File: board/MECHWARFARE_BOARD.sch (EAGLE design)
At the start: 8 parts, among them J1 5267-3, Q2 FDD4141TO252

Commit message: giving access to necessary libs
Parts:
- removed MS1: FEATHERWINGEXTENDED_BOTH_ENDS, ME507:FEATHERWINGEXTENDED_BOTH_ENDS
- removed TURRET_PWR1: XT60, XT60:XT60
- added MS2: FEATHERWINGEXTENDED_BOTH_ENDS, ME507:FEATHERWINGEXTENDED_BOTH_ENDS
- added U$1: XT60, XT60:XT60
- renumbered J1 to J2, TURRET_PWR to U$2
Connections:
- net GND: now also MS2.GND, U$1.GND; no longer MS1.GND, TURRET_PWR1.GND
- net MOTOR_CMD: now also MS2.GPIOTX; no longer MS1.GPIOTX
- net MOTOR_POWER: now also U$1.VCC; no longer TURRET_PWR1.VCC
- net N$21: now also MS2.GPIO5; no longer MS1.GPIO5
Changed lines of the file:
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@@
 </classes>
 <parts>
-<part name="FRAME1" library="ME507" deviceset="TITLEBLOCK_LET_L" device="">
-<attribute name="BOARD_NAME" value="ZEN GARDEN"/>
-</part>
 <part name="R1" library="rcl" library_urn="urn:adsk.eagle:library:334" deviceset="R-US_" device="R0805" package3d_urn="urn:adsk.eagle:package:23553/2" value="100"/>
 <part name="X_1" library="ngspice-simulation" library_urn="urn:adsk.eagle:library:527439" deviceset="GND" device=""/>
 <part name="D1" library="diode" library_urn="urn:adsk.eagle:library:210" deviceset="DIODE-" device="DO-214AC" package3d_urn="urn:adsk.eagle:package:43416/2"/>
-<part name="MS1" library="ME507" deviceset="FEATHERWING" device="EXTENDED_BOTH_ENDS"/>
-<part name="TURRET_PWR" library="XT60" deviceset="XT60" device=""/>
 <part name="X_2" library="ngspice-simulation" library_urn="urn:adsk.eagle:library:527439" deviceset="GND" device=""/>
 <part name="Q2" library="transistor-fet" library_urn="urn:adsk.eagle:library:396" deviceset="FDD4141" device="TO252" package3d_urn="urn:adsk.eagle:package:28537/2"/>
-<part name="TURRET_PWR1" library="XT60" deviceset="XT60" device=""/>
 <part name="X_3" library="ngspice-simulation" library_urn="urn:adsk.eagle:library:527439" deviceset="GND" device=""/>
 <part name="X3" library="ME507" deviceset="SCREWTERM_2P" device="_254"/>
 <part name="X_5" library="ngspice-simulation" library_urn="urn:adsk.eagle:library:527439" deviceset="GND" device=""/>
 <part name="X_4" library="ngspice-simulation" library_urn="urn:adsk.eagle:library:527439" deviceset="GND" device=""/>
-<part name="J1" library="con-molex-spox" deviceset="5267-3" device=""/>
+<part name="U$1" library="XT60" deviceset="XT60" device=""/>
+<part name="U$2" library="XT60" deviceset="XT60" device=""/>
+<part name="J2" library="con-molex-spox" deviceset="5267-3" device=""/>
+<part name="MS2" library="ME507" deviceset="FEATHERWING" device="EXTENDED_BOTH_ENDS"/>
+<part name="FRAME1" library="ME507" deviceset="TITLEBLOCK_LET_L" device="">
+<attribute name="AUTHOR" value="Aaron Tran"/>
+<attribute name="BOARD_NAME" value="MOT_AND_TURRET"/>
+<attribute name="PROJECT_NAME" value="MECH WARFARE"/>
+</part>
 </parts>
 <sheets>
@@
 </plain>
 <instances>
-<instance part="FRAME1" gate="G$3" x="0" y="0" smashed="yes"/>
-<instance part="FRAME1" gate="G$1" x="-5.08" y="0" smashed="yes"/>
-<instance part="FRAME1" gate="G$2" x="142.24" y="0" smashed="yes">
-<attribute name="LAST_DATE_TIME" x="154.94" y="11.43" size="2.54" layer="94"/>
-<attribute name="SHEET" x="184.15" y="6.35" size="2.54" layer="94"/>
-<attribute name="DRAWING_NAME" x="235.585" y="3.81" size="2.54" layer="94" align="bottom-right"/>
-<attribute name="REVISION" x="152.4" y="6.35" size="2.54" layer="94"/>
-<attribute name="PROJECT_NAME" x="160.02" y="30.48" size="2.54" layer="94"/>
-<attribute name="DOC_NUM" x="179.324" y="1.27" size="2.54" layer="94"/>
-<attribute name="AUTHOR" x="165.1" y="16.51" size="2.54" layer="94"/>
-<attribute name="BOARD_NAME" x="154.94" y="22.86" size="2.54" layer="94"/>
-</instance>
 <instance part="R1" gate="G$1" x="149.86" y="88.9" smashed="yes">
 <attribute name="NAME" x="146.05" y="90.3986" size="1.778" layer="95"/>
@@
 <attribute name="VALUE" x="190.2714" y="104.14" size="1.778" layer="96" rot="R90"/>
 </instance>
-<instance part="MS1" gate="G$1" x="96.52" y="127" smashed="yes" rot="R270"/>
-<instance part="TURRET_PWR" gate="G$1" x="175.26" y="116.84" smashed="yes" rot="R180"/>
 <instance part="X_2" gate="G$1" x="180.34" y="111.76" smashed="yes"/>
 <instance part="Q2" gate="G$1" x="185.42" y="86.36" smashed="yes">
@@
 <attribute name="NAME" x="173.99" y="85.09" size="1.778" layer="95"/>
 </instance>
-<instance part="TURRET_PWR1" gate="G$1" x="58.42" y="124.46" smashed="yes"/>
-<instance part="X_3" gate="G$1" x="38.1" y="124.46" smashed="yes"/>
+<instance part="X_3" gate="G$1" x="35.56" y="124.46" smashed="yes"/>
 <instance part="X3" gate="-1" x="231.14" y="104.14" smashed="yes">
 <attribute name="NAME" x="234.696" y="103.505" size="1.778" layer="95"/>
@@
 <instance part="X_5" gate="G$1" x="81.28" y="111.76" smashed="yes"/>
 <instance part="X_4" gate="G$1" x="33.02" y="101.6" smashed="yes"/>
-<instance part="J1" gate="G$1" x="38.1" y="88.9" smashed="yes" rot="R180">
+<instance part="U$1" gate="G$1" x="58.42" y="127" smashed="yes"/>
+<instance part="U$2" gate="G$1" x="175.26" y="116.84" smashed="yes" rot="R180"/>
+<instance part="J2" gate="G$1" x="38.1" y="88.9" smashed="yes" rot="R180">
 <attribute name="VALUE" x="38.1" y="94.38" size="1.27" layer="94" rot="R180"/>
 <attribute name="NAME" x="38.1" y="83.74" size="1.27" layer="94" rot="R180"/>
+</instance>
+<instance part="MS2" gate="G$1" x="99.06" y="127" smashed="yes" rot="R270"/>
+<instance part="FRAME1" gate="G$3" x="5.08" y="0" smashed="yes"/>
+<instance part="FRAME1" gate="G$1" x="0" y="0" smashed="yes"/>
+<instance part="FRAME1" gate="G$2" x="147.32" y="0" smashed="yes">
+<attribute name="LAST_DATE_TIME" x="160.02" y="11.43" size="2.54" layer="94"/>
+<attribute name="SHEET" x="189.23" y="6.35" size="2.54" layer="94"/>
+<attribute name="DRAWING_NAME" x="240.665" y="3.81" size="2.54" layer="94" align="bottom-right"/>
+<attribute name="REVISION" x="157.48" y="6.35" size="2.54" layer="94"/>
+<attribute name="PROJECT_NAME" x="165.1" y="30.48" size="2.54" layer="94"/>
+<attribute name="DOC_NUM" x="184.404" y="1.27" size="2.54" layer="94"/>
+<attribute name="AUTHOR" x="170.18" y="16.51" size="2.54" layer="94"/>
+<attribute name="BOARD_NAME" x="160.02" y="22.86" size="2.54" layer="94"/>
 </instance>
 </instances>
@@
 <label x="210.82" y="104.14" size="1.778" layer="95"/>
 <pinref part="D1" gate="G$1" pin="C"/>
-<pinref part="TURRET_PWR" gate="G$1" pin="VCC"/>
 <wire x1="203.2" y1="104.14" x2="228.6" y2="104.14" width="0.1524" layer="91"/>
 <wire x1="180.34" y1="119.38" x2="203.2" y2="119.38" width="0.1524" layer="91"/>
@@
 <junction x="203.2" y="104.14"/>
 <pinref part="X3" gate="-1" pin="1"/>
+<pinref part="U$2" gate="G$1" pin="VCC"/>
 </segment>
 </net>
@@
 </segment>
 <segment>
-<pinref part="TURRET_PWR" gate="G$1" pin="GND"/>
 <pinref part="X_2" gate="G$1" pin="0"/>
 <wire x1="180.34" y1="114.3" x2="180.34" y2="111.76" width="0.1524" layer="91"/>
 <label x="185.42" y="111.76" size="1.778" layer="95"/>
+<pinref part="U$2" gate="G$1" pin="GND"/>
 </segment>
 <segment>
-<pinref part="MS1" gate="G$1" pin="GND"/>
 <pinref part="X_5" gate="G$1" pin="0"/>
-<wire x1="91.44" y1="114.3" x2="81.28" y2="114.3" width="0.1524" layer="91"/>
+<wire x1="93.98" y1="114.3" x2="81.28" y2="114.3" width="0.1524" layer="91"/>
 <wire x1="81.28" y1="114.3" x2="81.28" y2="111.76" width="0.1524" layer="91"/>
 <label x="76.2" y="111.76" size="1.778" layer="95"/>
+<pinref part="MS2" gate="G$1" pin="GND"/>
 </segment>
 <segment>
 <pinref part="X_3" gate="G$1" pin="0"/>
-<pinref part="TURRET_PWR1" gate="G$1" pin="GND"/>
-<wire x1="38.1" y1="124.46" x2="38.1" y2="127" width="0.1524" layer="91"/>
-<wire x1="38.1" y1="127" x2="53.34" y2="127" width="0.1524" layer="91"/>
+<wire x1="35.56" y1="124.46" x2="35.56" y2="129.54" width="0.1524" layer="91"/>
+<wire x1="35.56" y1="129.54" x2="53.34" y2="129.54" width="0.1524" layer="91"/>
+<pinref part="U$1" gate="G$1" pin="GND"/>
 </segment>
 <segment>
@@
 <wire x1="33.02" y1="106.68" x2="33.02" y2="101.6" width="0.1524" layer="91"/>
 <pinref part="X_4" gate="G$1" pin="0"/>
-<pinref part="J1" gate="G$1" pin="-3"/>
 <wire x1="40.64" y1="91.36" x2="38.1" y2="91.36" width="0.1524" layer="91"/>
+<pinref part="J2" gate="G$1" pin="-3"/>
 </segment>
 </net>
@@
 <segment>
 <pinref part="R1" gate="G$1" pin="1"/>
-<pinref part="MS1" gate="G$1" pin="GPIO5"/>
-<wire x1="134.62" y1="88.9" x2="144.78" y2="88.9" width="0.1524" layer="91"/>
+<wire x1="137.16" y1="88.9" x2="144.78" y2="88.9" width="0.1524" layer="91"/>
+<pinref part="MS2" gate="G$1" pin="GPIO5"/>
 </segment>
 </net>
 <net name="MOTOR_POWER" class="0">
 <segment>
-<pinref part="TURRET_PWR1" gate="G$1" pin="VCC"/>
-<wire x1="53.34" y1="121.92" x2="48.26" y2="121.92" width="0.1524" layer="91"/>
-<pinref part="J1" gate="G$1" pin="-2"/>
+<wire x1="53.34" y1="124.46" x2="48.26" y2="124.46" width="0.1524" layer="91"/>
 <wire x1="38.1" y1="88.82" x2="38.1" y2="88.9" width="0.1524" layer="91"/>
 <wire x1="38.1" y1="88.9" x2="48.26" y2="88.9" width="0.1524" layer="91"/>
-<wire x1="48.26" y1="88.9" x2="48.26" y2="121.92" width="0.1524" layer="91"/>
+<wire x1="48.26" y1="88.9" x2="48.26" y2="124.46" width="0.1524" layer="91"/>
 <label x="50.8" y="106.68" size="1.778" layer="95"/>
+<pinref part="U$1" gate="G$1" pin="VCC"/>
+<pinref part="J2" gate="G$1" pin="-2"/>
 </segment>
 </net>
 <net name="MOTOR_CMD" class="0">
 <segment>
-<pinref part="J1" gate="G$1" pin="-1"/>
-<pinref part="MS1" gate="G$1" pin="GPIOTX"/>
 <wire x1="38.1" y1="86.28" x2="91.44" y2="86.28" width="0.1524" layer="91"/>
-<wire x1="91.44" y1="86.28" x2="91.44" y2="86.36" width="0.1524" layer="91"/>
+<wire x1="91.44" y1="86.28" x2="93.98" y2="86.36" width="0.1524" layer="91"/>
 <label x="50.8" y="83.82" size="1.778" layer="95"/>
+<pinref part="J2" gate="G$1" pin="-1"/>
+<pinref part="MS2" gate="G$1" pin="GPIOTX"/>
 </segment>
 </net>

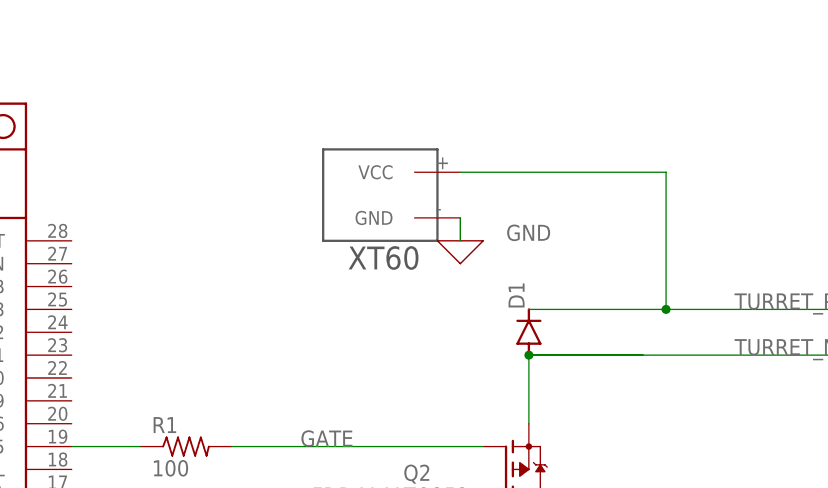
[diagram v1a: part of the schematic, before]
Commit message: Connector Change
Switched back to xt60 and removed duplicate files.
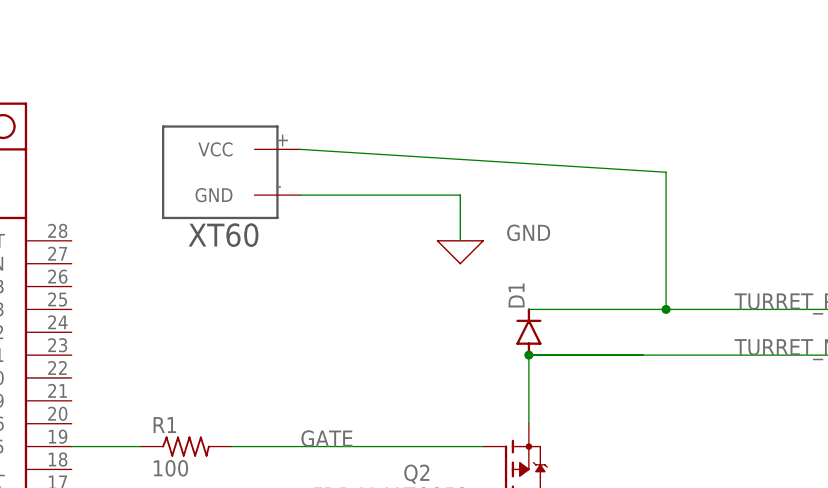
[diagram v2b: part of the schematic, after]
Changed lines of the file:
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@@
 <part name="X_4" library="ngspice-simulation" library_urn="urn:adsk.eagle:library:527439" deviceset="GND" device=""/>
 <part name="U$1" library="XT60" deviceset="XT60" device=""/>
-<part name="U$2" library="XT60" deviceset="XT60" device=""/>
 <part name="J2" library="con-molex-spox" deviceset="5267-3" device=""/>
 <part name="MS2" library="ME507" deviceset="FEATHERWING" device="EXTENDED_BOTH_ENDS"/>
@@
 <attribute name="PROJECT_NAME" value="MECH WARFARE"/>
 </part>
+<part name="U$2" library="XT60" deviceset="XT60" device=""/>
 </parts>
 <sheets>
@@
 <instance part="X_4" gate="G$1" x="33.02" y="101.6" smashed="yes"/>
 <instance part="U$1" gate="G$1" x="58.42" y="127" smashed="yes"/>
-<instance part="U$2" gate="G$1" x="175.26" y="116.84" smashed="yes" rot="R180"/>
 <instance part="J2" gate="G$1" x="38.1" y="88.9" smashed="yes" rot="R180">
 <attribute name="VALUE" x="38.1" y="94.38" size="1.27" layer="94" rot="R180"/>
@@
 <attribute name="BOARD_NAME" x="160.02" y="22.86" size="2.54" layer="94"/>
 </instance>
+<instance part="U$2" gate="G$1" x="157.48" y="119.38" smashed="yes" rot="R180"/>
 </instances>
 <busses>
@@
 <pinref part="D1" gate="G$1" pin="C"/>
 <wire x1="203.2" y1="104.14" x2="228.6" y2="104.14" width="0.1524" layer="91"/>
-<wire x1="180.34" y1="119.38" x2="203.2" y2="119.38" width="0.1524" layer="91"/>
+<wire x1="162.56" y1="121.92" x2="203.2" y2="119.38" width="0.1524" layer="91"/>
 <wire x1="203.2" y1="119.38" x2="203.2" y2="104.14" width="0.1524" layer="91"/>
 <junction x="203.2" y="104.14"/>
@@
 <segment>
 <pinref part="X_2" gate="G$1" pin="0"/>
-<wire x1="180.34" y1="114.3" x2="180.34" y2="111.76" width="0.1524" layer="91"/>
+<wire x1="180.34" y1="116.84" x2="180.34" y2="111.76" width="0.1524" layer="91"/>
 <label x="185.42" y="111.76" size="1.778" layer="95"/>
+<wire x1="180.34" y1="116.84" x2="162.56" y2="116.84" width="0.1524" layer="91"/>
 <pinref part="U$2" gate="G$1" pin="GND"/>
 </segment>
